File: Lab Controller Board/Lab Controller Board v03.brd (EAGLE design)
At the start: 50 x 50 mm, 37 parts, among them Q2 NPN - 2N5088, Q3 MOSFET-NCHANNELFQP30N06L, Q4 NPN - 2N5088, Q5 MOSFET-NCHANNELFQP30N06L, Q6 NPN - 2N5088, Q7 MOSFET-NCHANNELFQP30N06L, Q8 NPN - 2N5088, U1 ATMEGA328P_TQFP

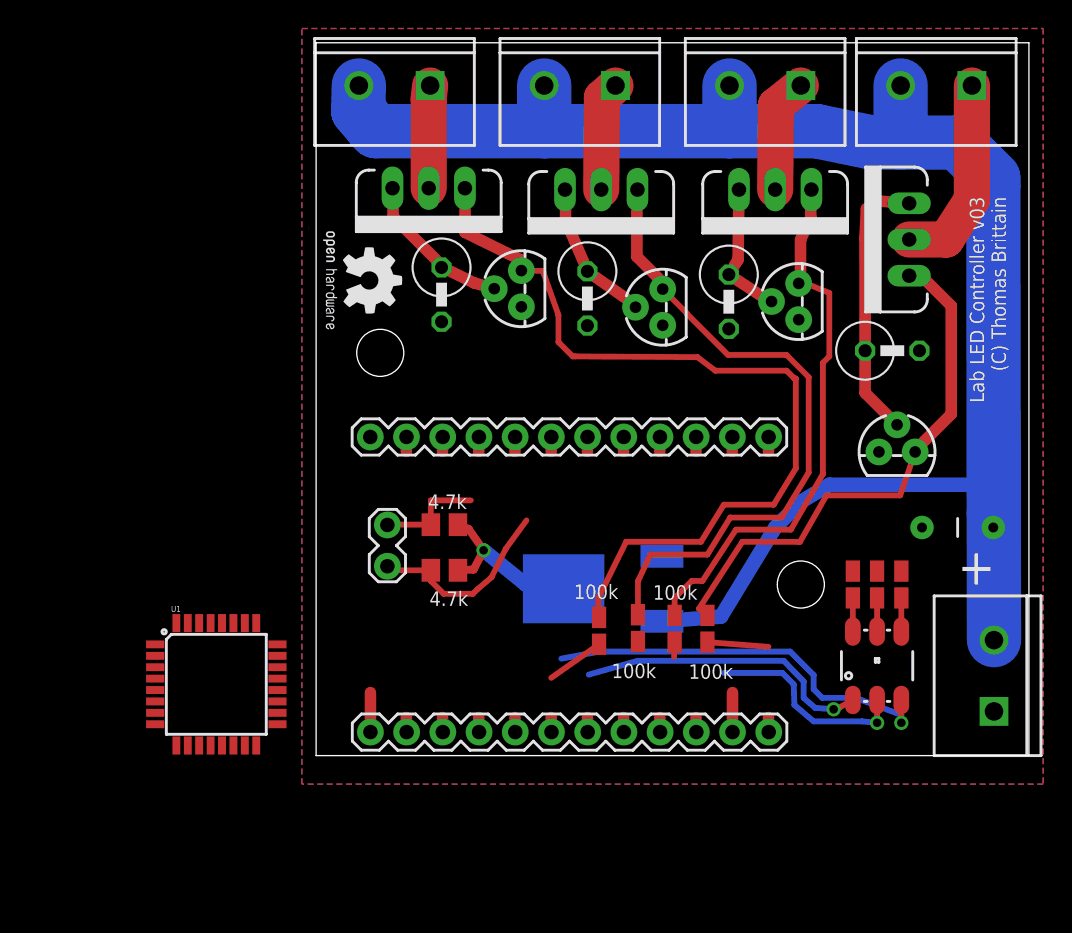
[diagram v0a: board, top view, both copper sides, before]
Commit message: SMD'ing the LAB Led Controller
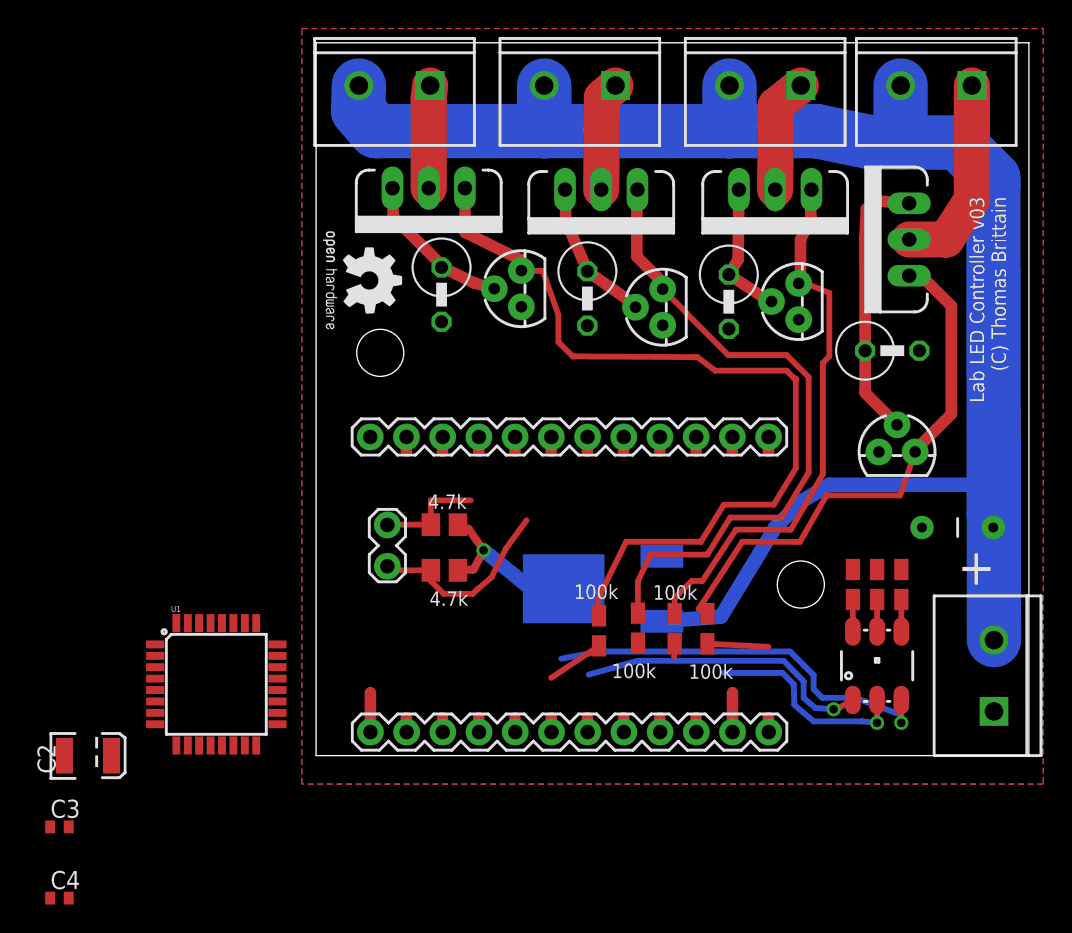
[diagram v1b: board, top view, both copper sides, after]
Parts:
- added C2: 10uF, SparkFun-Capacitors:EIA3528
- added C3, C4: 0.1uF, resistor:C0402
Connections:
- new net N$1: C3.1, U1.20
- new net VCC: C2.A, C4.1, MC7805CD2TR4.4, U1.4, U1.6
- net 5V: no longer MC7805CD2TR4.4, U1.4, U1.6
- net GND: now also C2.C, C3.2, C4.2, U1.21
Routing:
- net 5V: track 11.7 -> 9.06 mm
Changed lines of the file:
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@@
 <?xml version="1.0" encoding="utf-8"?>
 <!DOCTYPE eagle SYSTEM "eagle.dtd">
-<eagle version="7.3.0">
+<eagle version="7.5.0">
 <drawing>
 <settings>
@@
 <layer number="113" name="IDFDebug" color="7" fill="1" visible="yes" active="yes"/>
 <layer number="114" name="Badge_Outline" color="11" fill="1" visible="no" active="no"/>
+<layer number="115" name="ReferenceISLANDS" color="7" fill="1" visible="yes" active="yes"/>
 <layer number="116" name="Patch_BOT" color="9" fill="4" visible="yes" active="yes"/>
 <layer number="118" name="Rect_Pads" color="7" fill="1" visible="yes" active="yes"/>
@@
 <attribute name="PROD_ID" value="IC-09069" x="-7" y="5" size="1.778" layer="27" display="off"/>
 </element>
+<element name="C2" library="SparkFun-Capacitors" package="EIA3528" value="10uF" x="-16" y="0"/>
+<element name="C3" library="resistor" package="C0402" value="0.1uF" x="-18" y="-5"/>
+<element name="C4" library="resistor" package="C0402" value="0.1uF" x="-18" y="-10"/>
 </elements>
 <signals>
@@
 <contactref element="Q2" pad="3"/>
 <contactref element="R1" pad="2"/>
-<wire x1="22.574290625" y1="9.882603125" x2="22.574290625" y2="12.224290625" width="0.4064" layer="1"/>
+<wire x1="22.574290625" y1="9.995103125" x2="22.574290625" y2="12.224290625" width="0.4064" layer="1"/>
 <wire x1="22.574290625" y1="12.224290625" x2="23.45" y2="14.1" width="0.4064" layer="1"/>
 <wire x1="23.45" y1="14.1" x2="27.45" y2="14.1" width="0.4064" layer="1"/>
@@
 <contactref element="U1" pad="3"/>
 <contactref element="U1" pad="5"/>
+<contactref element="C2" pad="C"/>
+<contactref element="C3" pad="2"/>
+<contactref element="C4" pad="2"/>
+<contactref element="U1" pad="21"/>
 <wire x1="39.48" y1="21.3" x2="42.32" y2="28.4" width="0" layer="19" extent="1-1"/>
 <wire x1="42.5" y1="16" x2="39.48" y2="21.3" width="0" layer="19" extent="1-1"/>
-<wire x1="41.05" y1="12.94" x2="42.5" y2="16" width="0" layer="19" extent="1-1"/>
-<wire x1="39.35" y1="12.94" x2="41.05" y2="12.94" width="0" layer="19" extent="1-1"/>
-<wire x1="37.65" y1="12.94" x2="39.35" y2="12.94" width="0" layer="19" extent="1-1"/>
+<wire x1="41.05" y1="13.0525" x2="42.5" y2="16" width="0" layer="19" extent="1-1"/>
+<wire x1="39.35" y1="13.0525" x2="41.05" y2="13.0525" width="0" layer="19" extent="1-1"/>
+<wire x1="37.65" y1="13.0525" x2="39.35" y2="13.0525" width="0" layer="19" extent="1-1"/>
 <wire x1="33.85" y1="30.58" x2="42.32" y2="28.4" width="0" layer="19" extent="1-1"/>
 <wire x1="28.95" y1="29.93" x2="33.85" y2="30.58" width="0" layer="19" extent="1-1"/>
@@
 <wire x1="14.4" y1="31.48" x2="19.03" y2="30.16" width="0" layer="19" extent="1-1"/>
 <wire x1="8.8" y1="30.43" x2="14.4" y2="31.48" width="0" layer="19" extent="1-1"/>
-<wire x1="47.55" y1="3.1" x2="41.05" y2="12.94" width="0" layer="19" extent="1-1"/>
-<wire x1="24.26" y1="13.98" x2="37.65" y2="12.94" width="0" layer="19" extent="1-16"/>
-<wire x1="-11.2926" y1="6.2" x2="8.8" y2="30.43" width="0" layer="19" extent="1-1"/>
-<wire x1="-11.2926" y1="4.6" x2="-11.2926" y2="6.2" width="0" layer="19" extent="1-1"/>
+<wire x1="47.55" y1="3.1" x2="41.05" y2="13.0525" width="0" layer="19" extent="1-1"/>
+<wire x1="24.26" y1="13.98" x2="37.65" y2="13.0525" width="0" layer="19" extent="1-16"/>
+<wire x1="-2.7074" y1="5.4" x2="8.8" y2="30.43" width="0" layer="19" extent="1-1"/>
+<wire x1="-11.2926" y1="4.6" x2="-2.7074" y2="5.4" width="0" layer="19" extent="1-1"/>
+<wire x1="-11.2926" y1="6.2" x2="-11.2926" y2="4.6" width="0" layer="19" extent="1-1"/>
+<wire x1="-17.65" y1="0" x2="-11.2926" y2="4.6" width="0" layer="19" extent="1-1"/>
+<wire x1="-17.35" y1="-5" x2="-17.65" y2="0" width="0" layer="19" extent="1-1"/>
+<wire x1="-17.35" y1="-10" x2="-17.35" y2="-5" width="0" layer="19" extent="1-1"/>
 </signal>
 <signal name="RX">
@@
 <wire x1="16.49" y1="2.67" x2="16.51" y2="1.65" width="0.8128" layer="1"/>
 <contactref element="R3" pad="1"/>
-<wire x1="16.49" y1="5.45" x2="19.85" y2="7.81" width="0.4064" layer="1"/>
+<wire x1="16.49" y1="5.45" x2="19.85" y2="7.6975" width="0.4064" layer="1"/>
 <wire x1="16.49" y1="2.67" x2="16.49" y2="5.45" width="0" layer="19" extent="1-1"/>
 </signal>
@@
 <wire x1="21.57" y1="2.67" x2="21.59" y2="1.65" width="0.8128" layer="1"/>
 <contactref element="R1" pad="1"/>
-<wire x1="22.57" y1="7.9983125" x2="22.574290625" y2="8.002603125" width="0.4064" layer="1"/>
-<wire x1="21.57" y1="2.67" x2="22.574290625" y2="8.002603125" width="0" layer="19" extent="1-1"/>
+<wire x1="22.57" y1="7.9983125" x2="22.574290625" y2="7.890103125" width="0.4064" layer="1"/>
+<wire x1="21.57" y1="2.67" x2="22.574290625" y2="7.890103125" width="0" layer="19" extent="1-1"/>
 </signal>
 <signal name="APM_PIN_6">
@@
 <wire x1="24.11" y1="2.67" x2="24.13" y2="1.65" width="0.8128" layer="1"/>
 <contactref element="R7" pad="1"/>
-<wire x1="25.11" y1="6.92" x2="25.15" y2="7.96" width="0.4064" layer="1"/>
+<wire x1="25.11" y1="6.92" x2="25.15" y2="7.8475" width="0.4064" layer="1"/>
 <wire x1="24.11" y1="2.67" x2="25.11" y2="6.92" width="0" layer="19" extent="1-1"/>
 </signal>
@@
 <contactref element="JP6" pad="1"/>
 <contactref element="R5" pad="1"/>
-<wire x1="31.73" y1="7.63" x2="27.45" y2="7.96" width="0.4064" layer="1"/>
+<wire x1="31.73" y1="7.63" x2="27.45" y2="7.8475" width="0.4064" layer="1"/>
 <wire x1="31.73" y1="2.67" x2="31.75" y2="1.65" width="0.8128" layer="1"/>
 <wire x1="31.73" y1="2.67" x2="31.73" y2="7.63" width="0" layer="19" extent="1-1"/>
@@
 <wire x1="21.75" y1="15" x2="19.8" y2="11.05" width="0.4064" layer="1"/>
 <wire x1="19.8" y1="11.05" x2="19.8" y2="9.74" width="0.4064" layer="1"/>
-<wire x1="19.8" y1="9.74" x2="19.85" y2="9.69" width="0.4064" layer="1"/>
+<wire x1="19.8" y1="9.74" x2="19.85" y2="9.8025" width="0.4064" layer="1"/>
 <wire x1="18.2" y1="28" x2="26.75" y2="27.95" width="0.4064" layer="1"/>
 <wire x1="26.75" y1="27.95" x2="28" y2="27" width="0.4064" layer="1"/>
@@
 <wire x1="42.45" y1="33.65" x2="40.71" y2="33.65" width="0.8128" layer="1"/>
 <wire x1="40.71" y1="33.65" x2="41.6" y2="33.66" width="0.8128" layer="1"/>
-<wire x1="27.45" y1="9.84" x2="26.85" y2="10.3" width="0.4064" layer="1"/>
+<wire x1="27.45" y1="9.9525" x2="26.85" y2="10.3" width="0.4064" layer="1"/>
 <wire x1="26.85" y1="10.3" x2="29.9" y2="15" width="0.4064" layer="1"/>
 <wire x1="29.9" y1="15" x2="33.94" y2="14.99" width="0.4064" layer="1"/>
@@
 <contactref element="Q8" pad="3"/>
 <contactref element="R7" pad="2"/>
-<wire x1="25.15" y1="9.84" x2="25.15" y2="11.05" width="0.4064" layer="1"/>
+<wire x1="25.15" y1="9.9525" x2="25.15" y2="11.05" width="0.4064" layer="1"/>
 <wire x1="25.15" y1="11.05" x2="26.35" y2="12.25" width="0.4064" layer="1"/>
 <wire x1="26.35" y1="12.25" x2="27.1" y2="12.25" width="0.4064" layer="1"/>
@@
 <contactref element="R10" pad="2"/>
 <contactref element="R9" pad="2"/>
-<contactref element="MC7805CD2TR4" pad="4"/>
 <via x="11.75" y="14.4" extent="1-16" drill="0.6"/>
 <wire x1="11.75" y1="14.4" x2="10.7" y2="15.9" width="0.5588" layer="1"/>
@@
 <wire x1="9.95" y1="13" x2="11.05" y2="13.05" width="0.5588" layer="1"/>
 <wire x1="11.05" y1="13.05" x2="11.75" y2="14.4" width="0.5588" layer="1"/>
-<wire x1="17.362" y1="11.7" x2="14.7" y2="12" width="1.016" layer="16"/>
 <wire x1="14.7" y1="12" x2="11.75" y2="14.4" width="1.016" layer="16"/>
-<contactref element="U1" pad="4"/>
-<contactref element="U1" pad="6"/>
-<wire x1="-11.2926" y1="5.4" x2="9.95" y2="13" width="0" layer="19" extent="1-1"/>
-<wire x1="-11.2926" y1="3.8" x2="-11.2926" y2="5.4" width="0" layer="19" extent="1-1"/>
 </signal>
 <signal name="N$6">
 <contactref element="LED1" pad="4"/>
 <contactref element="R11" pad="2"/>
-<wire x1="41.05" y1="8.7" x2="41.05" y2="11.06" width="0.4064" layer="1"/>
+<wire x1="41.05" y1="8.7" x2="41.05" y2="10.9475" width="0.4064" layer="1"/>
 </signal>
 <signal name="N$8">
 <contactref element="R12" pad="2"/>
 <contactref element="LED1" pad="6"/>
-<wire x1="37.65" y1="8.7" x2="37.65" y2="11.06" width="0.4064" layer="1"/>
+<wire x1="37.65" y1="8.7" x2="37.65" y2="10.9475" width="0.4064" layer="1"/>
 </signal>
 <signal name="N$9">
 <contactref element="R13" pad="2"/>
 <contactref element="LED1" pad="5"/>
-<wire x1="39.35" y1="8.7" x2="39.35" y2="11.06" width="0.4064" layer="1"/>
+<wire x1="39.35" y1="8.7" x2="39.35" y2="10.9475" width="0.4064" layer="1"/>
 </signal>
 <signal name="9">
@@
 <wire x1="3.81" y1="4.42" x2="3.81" y2="1.65" width="0.8128" layer="1"/>
 </signal>
+<signal name="VCC">
+<contactref element="U1" pad="4"/>
+<contactref element="U1" pad="6"/>
+<contactref element="MC7805CD2TR4" pad="4"/>
+<contactref element="C2" pad="A"/>
+<contactref element="C4" pad="1"/>
+<wire x1="-11.2926" y1="5.4" x2="17.362" y2="11.7" width="0" layer="19" extent="1-16"/>
+<wire x1="-11.2926" y1="3.8" x2="-11.2926" y2="5.4" width="0" layer="19" extent="1-1"/>
+<wire x1="-14.35" y1="0" x2="-11.2926" y2="3.8" width="0" layer="19" extent="1-1"/>
+<wire x1="-18.65" y1="-10" x2="-14.35" y2="0" width="0" layer="19" extent="1-1"/>
+</signal>
+<signal name="N$1">
+<contactref element="U1" pad="20"/>
+<contactref element="C3" pad="1"/>
+<wire x1="-2.7074" y1="4.6" x2="-18.65" y2="-5" width="0" layer="19" extent="1-1"/>
+</signal>
 </signals>
